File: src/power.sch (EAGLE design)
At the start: 25 parts, among them CON1 PINHEAD_2X02-0877590414, CON2 PINHEAD_2X02-0877590414, CON3 PINHEAD_2X02-0877590414, CON4 PINHEAD_2X02-0877590414, CON5 PINHEAD_2X02-0877590414, CON6 PINHEAD_2X04-SMD-2-MALE, CON7 PINHEAD_2X02-0877590414, IC1 UCC27282-SOIC8, IC2 UCC27282-SOIC8, IC3 UCC27282-SOIC8

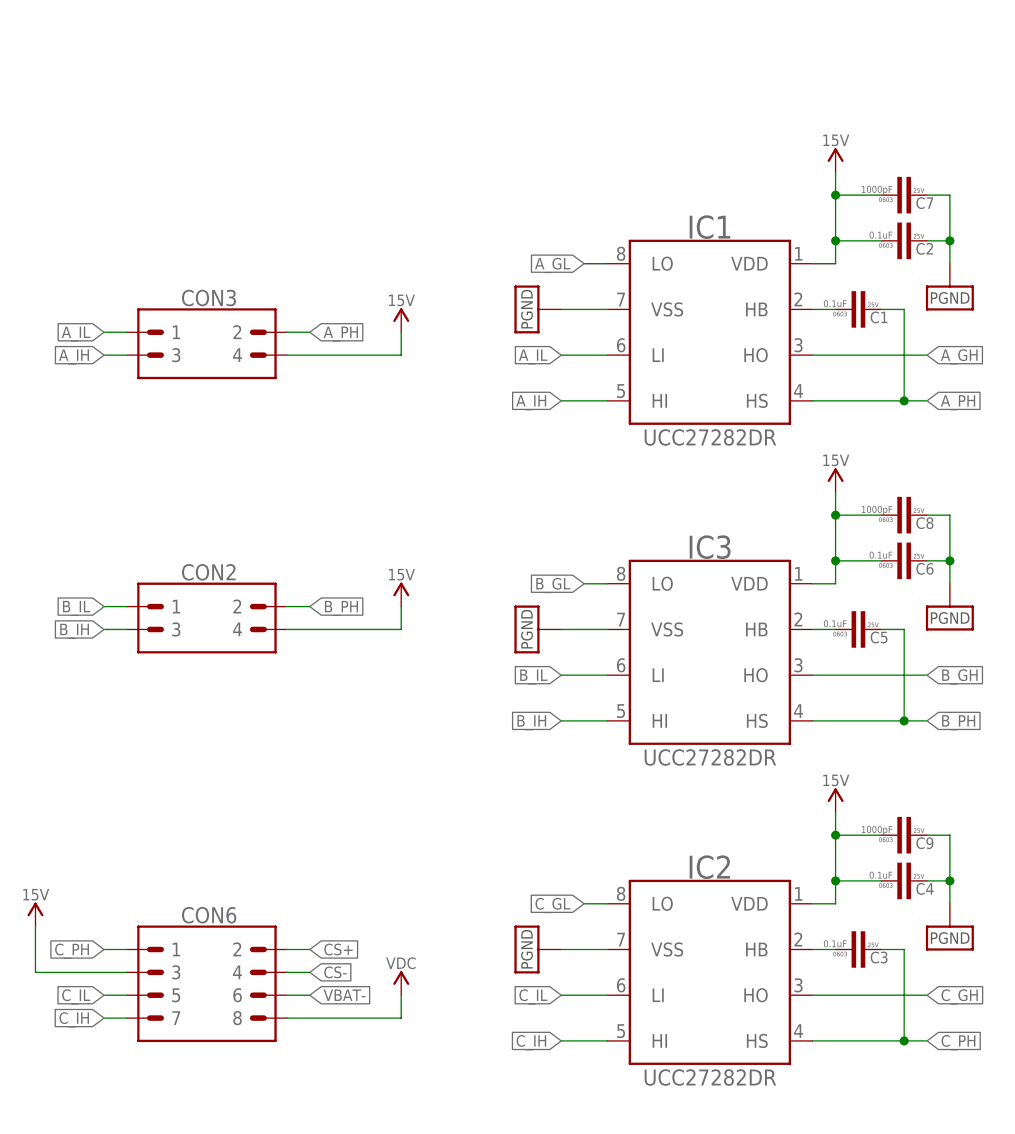
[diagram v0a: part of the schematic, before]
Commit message: Power PCB update
DRC  errors resolvinnng
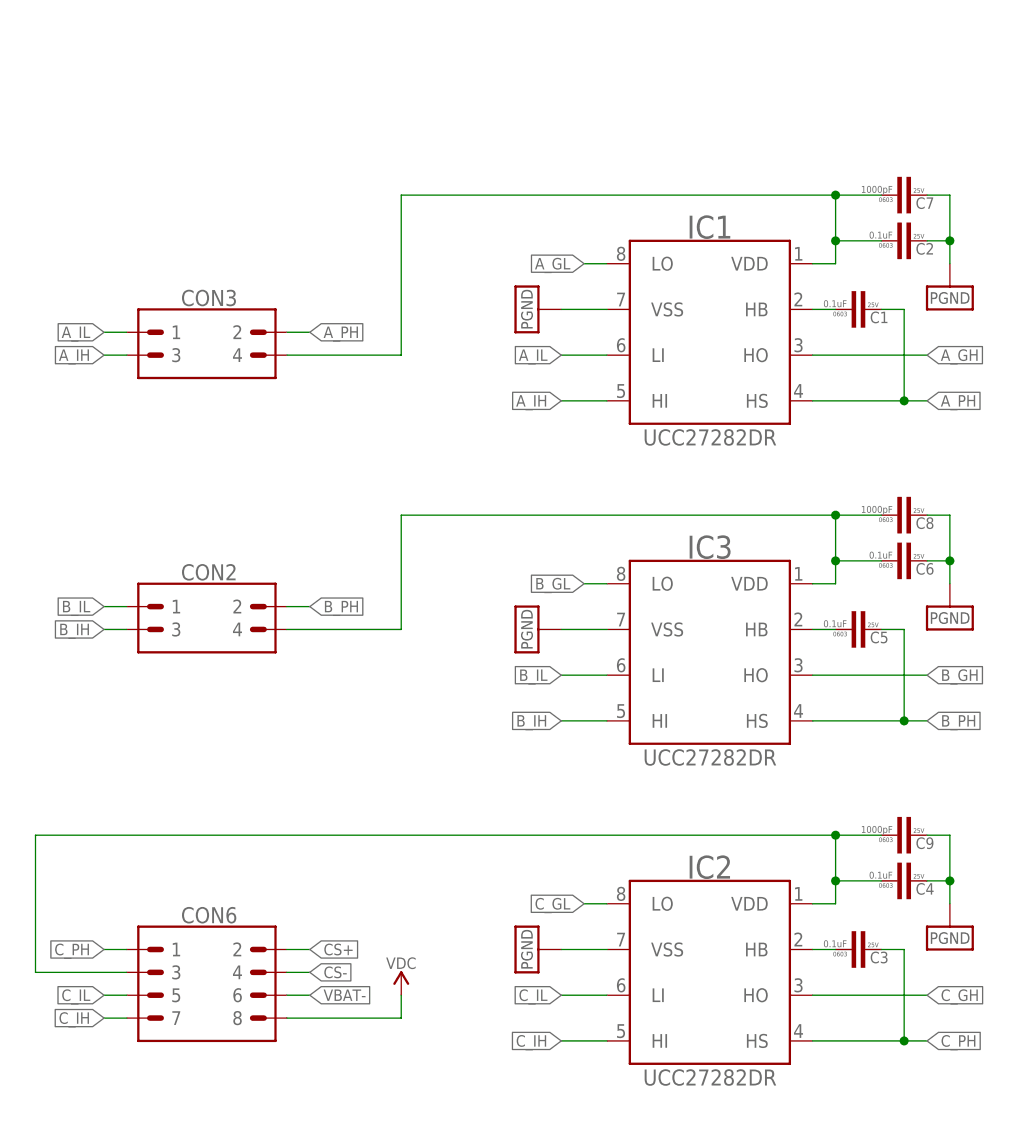
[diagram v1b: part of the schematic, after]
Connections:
- removed net VDD_15V: C2.1, C4.1, C6.1, C7.1, C8.1, C9.1, CON2.4, CON3.4, CON6.3, IC1.VDD, IC2.VDD, IC3.VDD
- new net 97: C2.1, C7.1, CON3.4, IC1.VDD
- new net N$3: C4.1, C9.1, CON6.3, IC2.VDD
- new net N$4: C6.1, C8.1, CON2.4, IC3.VDD

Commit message: Update power.sch
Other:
- note added: "MOSFET drivers should be supplied with 12V power line"
- moved on the sheet: C1, C2, C3, C4, C5, C6, C7, C8, C9, CON2, CON3, CON6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

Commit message: massibe attribute updates everywhere
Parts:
- C7, C8, C9: DIGIKEY# 1276-1006-1-ND -> 1276-1018-1-ND; MANF# CL10B104KA8NNNC -> CL10B102KB8NNNC; VOLTAGE 25V -> 50V
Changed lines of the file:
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@@
 <part name="C7" library="rc" library_urn="urn:adsk.eagle:library:2539423" deviceset="C" device="-0603" package3d_urn="urn:adsk.eagle:package:2539457/2" value="1000pF">
 <attribute name="AEC-Q" value="---"/>
-<attribute name="DIGIKEY#" value="1276-1006-1-ND"/>
+<attribute name="DIGIKEY#" value="1276-1018-1-ND"/>
 <attribute name="MANF" value="Samsung Electro-Mechanics"/>
-<attribute name="MANF#" value="CL10B104KA8NNNC"/>
+<attribute name="MANF#" value="CL10B102KB8NNNC"/>
 <attribute name="OPERATING_TEMP" value="-55°C ~ 125°C"/>
-<attribute name="VOLTAGE" value="25V"/>
+<attribute name="VOLTAGE" value="50V"/>
 </part>
 <part name="C8" library="rc" library_urn="urn:adsk.eagle:library:2539423" deviceset="C" device="-0603" package3d_urn="urn:adsk.eagle:package:2539457/2" value="1000pF">
 <attribute name="AEC-Q" value="---"/>
-<attribute name="DIGIKEY#" value="1276-1006-1-ND"/>
+<attribute name="DIGIKEY#" value="1276-1018-1-ND"/>
 <attribute name="MANF" value="Samsung Electro-Mechanics"/>
-<attribute name="MANF#" value="CL10B104KA8NNNC"/>
+<attribute name="MANF#" value="CL10B102KB8NNNC"/>
 <attribute name="OPERATING_TEMP" value="-55°C ~ 125°C"/>
-<attribute name="VOLTAGE" value="25V"/>
+<attribute name="VOLTAGE" value="50V"/>
 </part>
 <part name="C9" library="rc" library_urn="urn:adsk.eagle:library:2539423" deviceset="C" device="-0603" package3d_urn="urn:adsk.eagle:package:2539457/2" value="1000pF">
 <attribute name="AEC-Q" value="---"/>
-<attribute name="DIGIKEY#" value="1276-1006-1-ND"/>
+<attribute name="DIGIKEY#" value="1276-1018-1-ND"/>
 <attribute name="MANF" value="Samsung Electro-Mechanics"/>
-<attribute name="MANF#" value="CL10B104KA8NNNC"/>
+<attribute name="MANF#" value="CL10B102KB8NNNC"/>
 <attribute name="OPERATING_TEMP" value="-55°C ~ 125°C"/>
-<attribute name="VOLTAGE" value="25V"/>
+<attribute name="VOLTAGE" value="50V"/>
 </part>
 </parts>

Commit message: Interpcb connectors updated. Ground problem solved
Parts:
- removed CON3: PINHEAD_2X02-0877590414, pinhead:PINHEAD_2X02-0877590414
- added CON8: PINHEAD_2X03-0877590614, pinhead:PINHEAD_2X03-0877590614
- CON2: value PINHEAD_2X02-0877590414 -> PINHEAD_2X03-0877590614; device pinhead:PINHEAD_2X02-0877590414 -> pinhead:PINHEAD_2X03-0877590614
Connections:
- new net GND: C2.2, C6.2, C7.2, C8.2, CON2.1, CON8.1, IC1.VSS, IC3.VSS
- net 97: now also CON8.6; no longer CON3.4
- net A_IH: now also CON8.5; no longer CON3.3
- net A_IL: now also CON8.3; no longer CON3.1
- net A_PH: now also CON8.4; no longer CON3.2
- net B_IH: now also CON2.5; no longer CON2.3
- net B_IL: now also CON2.3; no longer CON2.1
- net B_PH: now also CON2.4; no longer CON2.2
- net N$4: now also CON2.6; no longer CON2.4
- net PGND: no longer C2.2, C4.2, C6.2, C7.2, C8.2, C9.2, IC1.VSS, IC2.VSS, IC3.VSS
- net VBAT-: now also C4.2, C9.2, IC2.VSS

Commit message: Massive routing update
InterPCB connectors between Cap PCB and power PCB replaced with bigger ones
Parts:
- CON1, CON4, CON5, CON7: value PINHEAD_2X02-0877590414 -> PINHEAD_2X02-SMD-2.54-MALE; device pinhead:PINHEAD_2X02-0877590414 -> pinhead:PINHEAD_2X02-SMD-2.54-MALE
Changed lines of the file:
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@@
 <attribute name="LCSC#" value="C469432"/>
 </part>
-<part name="CON1" library="pinhead" library_urn="urn:adsk.eagle:library:2540341" deviceset="PINHEAD_2X02" device="-0877590414" package3d_urn="urn:adsk.eagle:package:23512771/2" value="PINHEAD_2X02-0877590414"/>
-<part name="CON5" library="pinhead" library_urn="urn:adsk.eagle:library:2540341" deviceset="PINHEAD_2X02" device="-0877590414" package3d_urn="urn:adsk.eagle:package:23512771/2" value="PINHEAD_2X02-0877590414"/>
+<part name="CON1" library="pinhead" library_urn="urn:adsk.eagle:library:2540341" deviceset="PINHEAD_2X02" device="-SMD-2.54-MALE" package3d_urn="urn:adsk.eagle:package:24450034/3" value="PINHEAD_2X02-SMD-2.54-MALE"/>
+<part name="CON5" library="pinhead" library_urn="urn:adsk.eagle:library:2540341" deviceset="PINHEAD_2X02" device="-SMD-2.54-MALE" package3d_urn="urn:adsk.eagle:package:24450034/3" value="PINHEAD_2X02-SMD-2.54-MALE"/>
 <part name="+P6" library="supply_symbols" library_urn="urn:adsk.eagle:library:5017758" deviceset="VDC" device=""/>
 <part name="+P7" library="supply_symbols" library_urn="urn:adsk.eagle:library:5017758" deviceset="VDC" device=""/>
 <part name="CON6" library="pinhead" library_urn="urn:adsk.eagle:library:2540341" deviceset="PINHEAD_2X04" device="-SMD-2-MALE" package3d_urn="urn:adsk.eagle:package:23791919/2"/>
 <part name="+P10" library="supply_symbols" library_urn="urn:adsk.eagle:library:5017758" deviceset="VDC" device=""/>
-<part name="CON4" library="pinhead" library_urn="urn:adsk.eagle:library:2540341" deviceset="PINHEAD_2X02" device="-0877590414" package3d_urn="urn:adsk.eagle:package:23512771/2" value="PINHEAD_2X02-0877590414"/>
+<part name="CON4" library="pinhead" library_urn="urn:adsk.eagle:library:2540341" deviceset="PINHEAD_2X02" device="-SMD-2.54-MALE" package3d_urn="urn:adsk.eagle:package:24450034/3" value="PINHEAD_2X02-SMD-2.54-MALE"/>
 <part name="+P11" library="supply_symbols" library_urn="urn:adsk.eagle:library:5017758" deviceset="VDC" device=""/>
 <part name="+P12" library="supply_symbols" library_urn="urn:adsk.eagle:library:5017758" deviceset="VDC" device=""/>
-<part name="CON7" library="pinhead" library_urn="urn:adsk.eagle:library:2540341" deviceset="PINHEAD_2X02" device="-0877590414" package3d_urn="urn:adsk.eagle:package:23512771/2" value="PINHEAD_2X02-0877590414"/>
+<part name="CON7" library="pinhead" library_urn="urn:adsk.eagle:library:2540341" deviceset="PINHEAD_2X02" device="-SMD-2.54-MALE" package3d_urn="urn:adsk.eagle:package:24450034/3" value="PINHEAD_2X02-SMD-2.54-MALE"/>
 <part name="C7" library="rc" library_urn="urn:adsk.eagle:library:2539423" deviceset="C" device="-0603" package3d_urn="urn:adsk.eagle:package:2539457/2" value="1000pF">
 <attribute name="AEC-Q" value="---"/>
